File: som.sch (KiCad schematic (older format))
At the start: 39 parts, among them T2 BSS138APW, T4 BSS138APW, T5 BSS138APW

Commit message: Finish routing, cleanup silks
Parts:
- removed R112: R_110k_0603, jetson-nano-baseboard-footprints:0603-res, symbol jetson-nano-baseboard:R_110k_0603
- added R112: R_100k_0402, antmicro-footprints:0402-res, symbol antmicroResistors0402:R_100k_0402
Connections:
- net 1V8_SYS: now also R112.1
- net USR_BUTTON: now also R112.2
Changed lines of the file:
@@
 Wire Wire Line
 	11525 4075 11525 4025
-$Comp
-L jetson-nano-baseboard:R_110k_0603 R112
-U 1 1 62D721E3
-P 12450 7475
-F 0 "R112" V 12500 7175 60  0000 L CNN
-F 1 "R_110k_0603" H 12450 7325 60  0001 C CNN
-F 2 "jetson-nano-baseboard-footprints:0603-res" H 12650 7675 60  0001 L CNN
-F 3 "" H 12450 7475 50  0001 C CNN
-F 4 "TE" H 12650 7875 60  0001 L CNN "Manufacturer"
-F 5 "CPF0603B110KE1" H 12650 7775 60  0001 L CNN "MPN"
-F 6 "110k" V 12400 7225 50  0000 L CNN "Val"
-	1    12450 7475
-	0    -1   -1   0
-$EndComp
 Wire Wire Line
 	12125 7675 12450 7675
@@
 USR_BUTTON
 NoConn ~ 1875 10550
+$Comp
+L antmicroResistors0402:R_100k_0402 R112
+U 1 1 61ED8249
+P 12450 7475
+F 0 "R112" V 12405 7545 60  0000 L CNN
+F 1 "R_100k_0402" H 12450 7325 60  0001 C CNN
+F 2 "antmicro-footprints:0402-res" H 12650 7675 60  0001 L CNN
+F 3 "" H 12450 7475 50  0001 C CNN
+F 4 "VISHAY" H 12650 7875 60  0001 L CNN "Manufacturer"
+F 5 "CRCW0402100KFKEDHP" H 12650 7775 60  0001 L CNN "MPN"
+F 6 "100k" V 12503 7545 50  0000 L CNN "Val"
+	1    12450 7475
+	0    1    1    0
+$EndComp
 $EndSCHEMATC

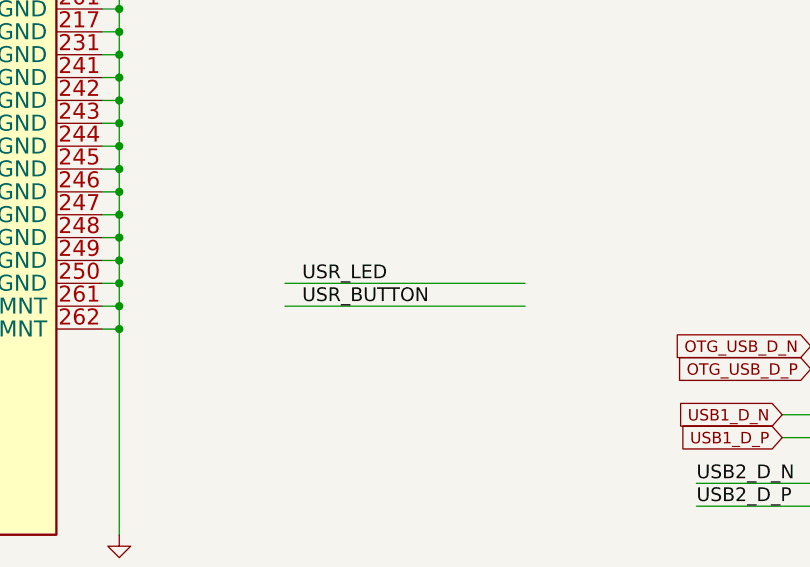
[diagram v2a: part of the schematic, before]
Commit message: Add comment to Usr led and button
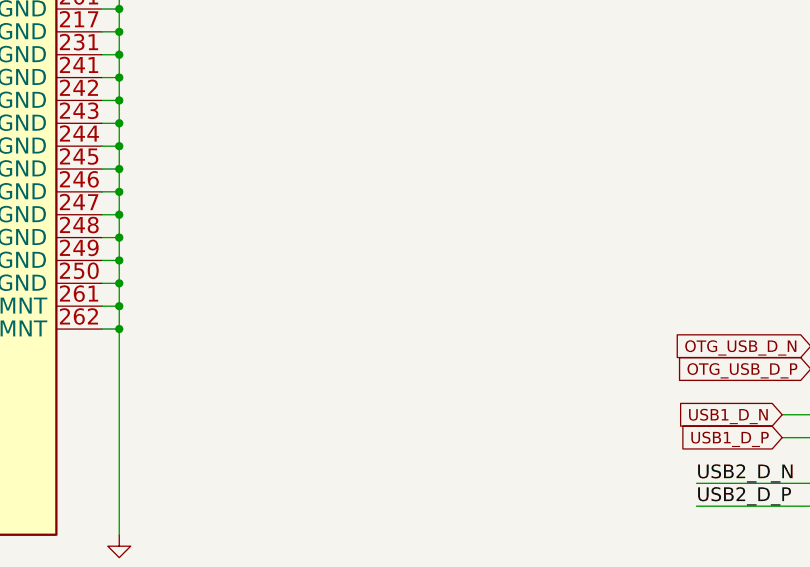
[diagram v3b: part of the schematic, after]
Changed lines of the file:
@@
 Text GLabel 4750 1875 2    50   Input ~ 0
 FAN_TACH
-Text Label 4725 5075 0    60   ~ 0
-USR_BUTTON
-Text Label 4725 4975 0    60   ~ 0
-USR_LED
 $Comp
 L jetson-nano-baseboard:Testpad TP13
@@
 	0    -1   1    0
 $EndComp
-Wire Wire Line
-	4650 4975 5700 4975
-Wire Wire Line
-	4650 5075 5700 5075
 Text GLabel 4625 2875 2    50   Input ~ 0
 FAN_PWM

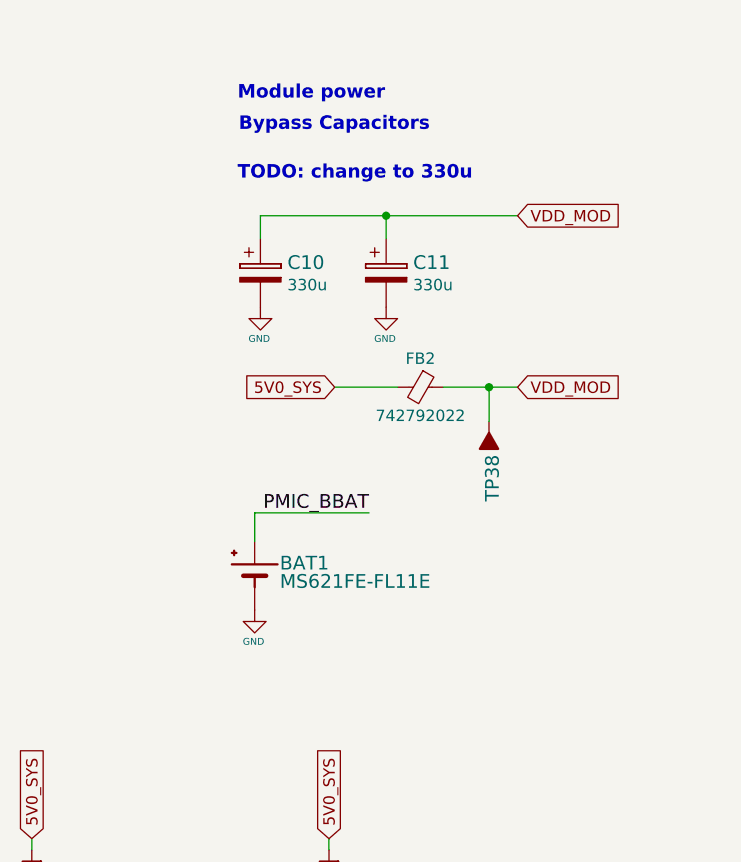
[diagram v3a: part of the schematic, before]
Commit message: Update MPS for FB2 FB3
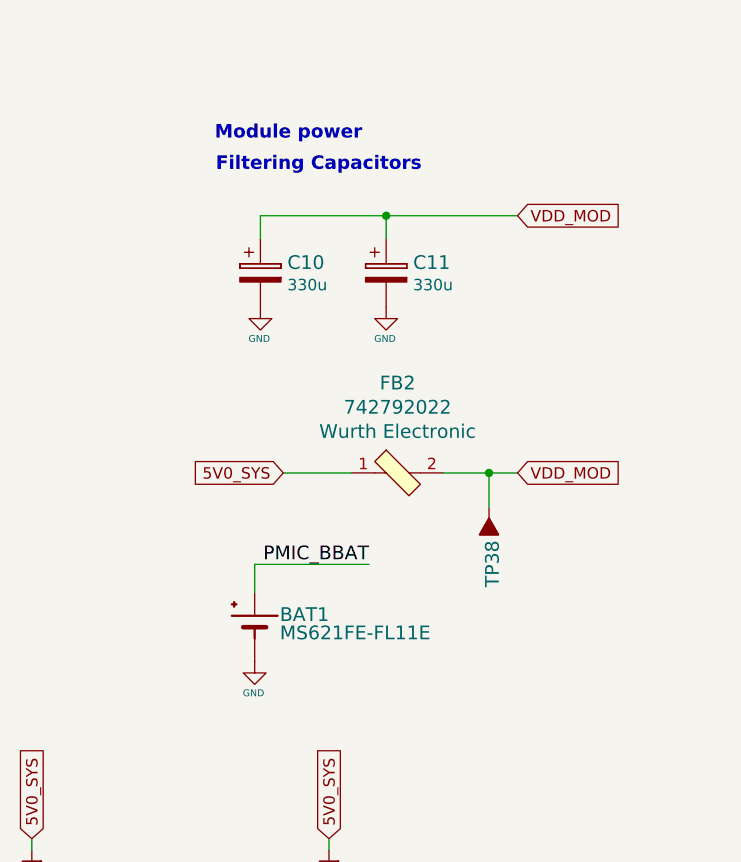
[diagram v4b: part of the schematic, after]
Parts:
- removed FB2: 742792022, jetson-nano-baseboard-footprints:0805-cap, symbol jetson-nano-baseboard:Ferrite_Bead_Small
- added FB2: 742792022, antmicro-footprints:0805-res, symbol antmicroFerriteBeadsandChips:742792022
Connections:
- net 5V0_SYS: now also FB2.1
- net VDD_MOD: now also FB2.2
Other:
- note added: "Filtering Capacitors"
- note removed: "Bypass Capacitors"
- note removed: "TODO: change to 330u"
- moved on the sheet: BAT1, TP38
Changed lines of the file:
@@
 Text Notes 13555 8337 0    59   ~ 12
 Mounting studs
-Text Notes 13705 937  0    59   ~ 12
-Bypass Capacitors
+Text Notes 13605 1112 0    59   ~ 12
+Filtering Capacitors
 Text Notes 11405 6037 0    59   ~ 12
 System Buttons
 Text Notes 11255 3562 0    59   ~ 12
 System Status
-Text Notes 13700 800  0    59   ~ 12
+Text Notes 13600 975  0    59   ~ 12
 Module power
 Text Label 750  8350 0    60   ~ 0
@@
 Text Label 3925 1275 0    60   ~ 0
 PMIC_BBAT
-Text Label 14275 2600 2    60   ~ 0
+Text Label 14275 2825 2    60   ~ 0
 PMIC_BBAT
 Text Label 10525 2075 0    60   ~ 0
@@
 Text GLabel 11300 1125 1    50   Input ~ 0
 3V3_SYS
-Text GLabel 14125 2050 0    50   Input ~ 0
+Text GLabel 13900 2425 0    50   Input ~ 0
 5V0_SYS
 Text GLabel 13650 9225 0    50   Input ~ 0
@@
 Text GLabel 1625 950  1    50   Input ~ 0
 VDD_MOD
-Text GLabel 14925 2050 2    50   Input ~ 0
+Text GLabel 14925 2425 2    50   Input ~ 0
 VDD_MOD
 $Comp
@@
 L jetson-nano-baseboard:GND #GND_0161
 U 1 1 5E710416
-P 13775 3025
-F 0 "#GND_0161" H 13775 3025 20  0001 C CNN
-F 1 "GND" H 13770 2887 30  0000 C CNN
-F 2 "" H 13775 3025 70  0001 C CNN
-F 3 "" H 13775 3025 70  0001 C CNN
-	1    13775 3025
+P 13775 3250
+F 0 "#GND_0161" H 13775 3250 20  0001 C CNN
+F 1 "GND" H 13770 3112 30  0000 C CNN
+F 2 "" H 13775 3250 70  0001 C CNN
+F 3 "" H 13775 3250 70  0001 C CNN
+	1    13775 3250
 	1    0    0    -1
 $EndComp
@@
 L jetson-nano-baseboard:Testpad TP38
 U 1 1 5E710405
-P 14800 2250
-F 0 "TP38" V 14750 2550 60  0000 R TNN
-F 1 "~" H 14800 2250 50  0001 C CNN
-F 2 "jetson-nano-baseboard-footprints:TP-R-1.5" H 14800 2250 50  0001 C CNN
-F 3 "" H 14800 2250 50  0001 C CNN
-F 4 "N/A" H -6880 -6362 50  0001 C CNN "MPN"
-F 5 "N/A" H -6880 -6362 50  0001 C CNN "Manufacturer"
-	1    14800 2250
+P 14800 2625
+F 0 "TP38" V 14750 2925 60  0000 R TNN
+F 1 "~" H 14800 2625 50  0001 C CNN
+F 2 "jetson-nano-baseboard-footprints:TP-R-1.5" H 14800 2625 50  0001 C CNN
+F 3 "" H 14800 2625 50  0001 C CNN
+F 4 "N/A" H -6880 -5987 50  0001 C CNN "MPN"
+F 5 "N/A" H -6880 -5987 50  0001 C CNN "Manufacturer"
+	1    14800 2625
 	-1   0    0    1
 $EndComp
@@
 L jetson-nano-baseboard:battery BAT1
 U 1 1 5E7103F0
-P 13775 2825
-F 0 "BAT1" H 13885 2795 60  0000 L BNN
-F 1 "MS621FE-FL11E" H 13885 2715 60  0000 L BNN
-F 2 "jetson-nano-baseboard-footprints:MS621FE-FL11E" H 13885 2715 60  0001 C CNN
-F 3 "" H 13885 2715 60  0001 C CNN
-F 4 "MS621FE-FL11E" H -2705 -7037 50  0001 C CNN "MPN"
-F 5 "Seiko" H -2705 -7037 50  0001 C CNN "Manufacturer"
-	1    13775 2825
+P 13775 3050
+F 0 "BAT1" H 13885 3020 60  0000 L BNN
+F 1 "MS621FE-FL11E" H 13885 2940 60  0000 L BNN
+F 2 "jetson-nano-baseboard-footprints:MS621FE-FL11E" H 13885 2940 60  0001 C CNN
+F 3 "" H 13885 2940 60  0001 C CNN
+F 4 "MS621FE-FL11E" H -2705 -6812 50  0001 C CNN "MPN"
+F 5 "Seiko" H -2705 -6812 50  0001 C CNN "Manufacturer"
+	1    13775 3050
 	1    0    0    -1
 $EndComp
@@
 Wire Wire Line
 	1625 1075 1625 950
-Text Notes 13700 1150 0    59   ~ 12
-TODO: change to 330u
 Wire Wire Line
 	3850 1575 4600 1575
@@
 	3850 1075 4825 1075
 Wire Wire Line
-	14800 2200 14800 2050
-Connection ~ 14800 2050
-Wire Wire Line
-	14800 2050 14925 2050
-Wire Wire Line
-	13775 2725 13775 2600
-Wire Wire Line
-	13775 2600 14275 2600
+	14800 2575 14800 2425
+Connection ~ 14800 2425
+Wire Wire Line
+	14800 2425 14925 2425
+Wire Wire Line
+	13775 2950 13775 2825
+Wire Wire Line
+	13775 2825 14275 2825
 Wire Wire Line
 	13650 9225 13725 9225
@@
 	14650 5200 14750 5200
 Wire Wire Line
-	14125 2050 14400 2050
-Wire Wire Line
-	14600 2050 14800 2050
-$Comp
-L jetson-nano-baseboard:Ferrite_Bead_Small FB?
-U 1 1 618512B9
-P 14500 2050
-AR Path="/608DC6E9/618512B9" Ref="FB?"  Part="1"
-AR Path="/610ACCAB/618512B9" Ref="FB2"  Part="1"
-F 0 "FB2" V 14375 2050 50  0000 C CNN
-F 1 "742792022 " V 14625 2050 50  0000 C CNN
-F 2 "jetson-nano-baseboard-footprints:0805-cap" V 14430 2050 50  0001 C CNN
-F 3 "~" H 14500 2050 50  0001 C CNN
-	1    14500 2050
-	0    1    1    0
-$EndComp
+	13900 2425 14200 2425
+Wire Wire Line
+	14600 2425 14800 2425
 $Comp
 L jetson-nano-baseboard:SPACER SP6
@@
 	0    1    1    0
 $EndComp
+$Comp
+L antmicroFerriteBeadsandChips:742792022 FB2
+U 1 1 6201B686
+P 14400 2425
+F 0 "FB2" H 14400 2818 60  0000 C CNN
+F 1 "742792022" H 14400 2606 60  0001 C CNN
+F 2 "antmicro-footprints:0805-res" H 14600 2625 60  0001 L CNN
+F 3 "https://www.we-online.com/katalog/datasheet/742792022.pdf" H 14600 2725 60  0001 L CNN
+F 4 "742792022" H 14400 2712 60  0000 C CNN "MPN"
+F 5 "Wurth Electronic" H 14400 2606 60  0000 C CNN "Manufacturer"
+	1    14400 2425
+	1    0    0    -1
+$EndComp
 $EndSCHEMATC

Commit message: Update libraries
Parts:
- FB2: footprint antmicro-footprints:0805-res -> jetson-nano-baseboard-footprints:0805-res; symbol antmicroFerriteBeadsandChips:742792022 -> jetson-nano-baseboard:742792022
- R112: footprint antmicro-footprints:0402-res -> jetson-nano-baseboard-footprints:0402-res; symbol antmicroResistors0402:R_100k_0402 -> jetson-nano-baseboard:R_100k_0402
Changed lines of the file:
@@
 NoConn ~ 1875 10550
 $Comp
-L antmicroResistors0402:R_100k_0402 R112
+L jetson-nano-baseboard:R_100k_0402 R112
 U 1 1 61ED8249
 P 12450 7475
 F 0 "R112" V 12405 7545 60  0000 L CNN
 F 1 "R_100k_0402" H 12450 7325 60  0001 C CNN
-F 2 "antmicro-footprints:0402-res" H 12650 7675 60  0001 L CNN
+F 2 "jetson-nano-baseboard-footprints:0402-res" H 12650 7675 60  0001 L CNN
 F 3 "" H 12450 7475 50  0001 C CNN
 F 4 "VISHAY" H 12650 7875 60  0001 L CNN "Manufacturer"
@@
 $EndComp
 $Comp
-L antmicroFerriteBeadsandChips:742792022 FB2
+L jetson-nano-baseboard:742792022 FB2
 U 1 1 6201B686
 P 14400 2425
 F 0 "FB2" H 14400 2818 60  0000 C CNN
 F 1 "742792022" H 14400 2606 60  0001 C CNN
-F 2 "antmicro-footprints:0805-res" H 14600 2625 60  0001 L CNN
+F 2 "jetson-nano-baseboard-footprints:0805-res" H 14600 2625 60  0001 L CNN
 F 3 "https://www.we-online.com/katalog/datasheet/742792022.pdf" H 14600 2725 60  0001 L CNN
 F 4 "742792022" H 14400 2712 60  0000 C CNN "MPN"
